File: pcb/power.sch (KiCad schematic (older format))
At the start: 25 parts, among them U16 AP22811AW5-7‎, U17 AP61302, U18 LP5907MFX-3.3, U4 AP61302

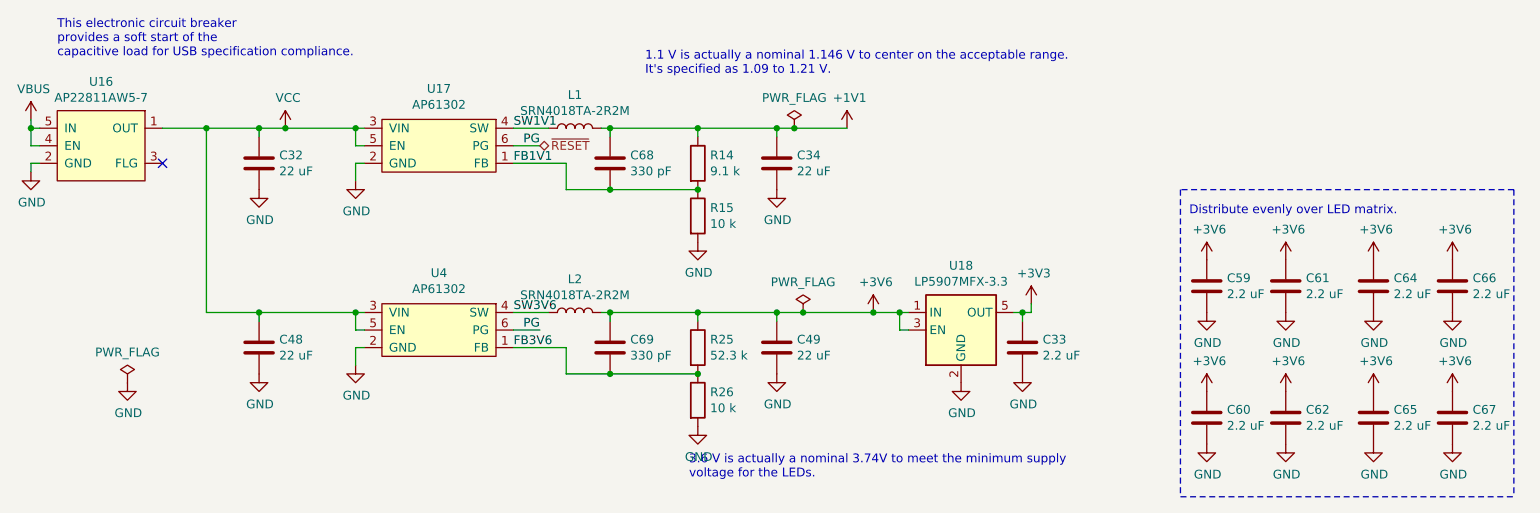
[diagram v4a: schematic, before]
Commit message: use AP3441LSHE-7B DC-DC switching to available part from long lead time part adds 2 22 uF 0805 capacitors as well
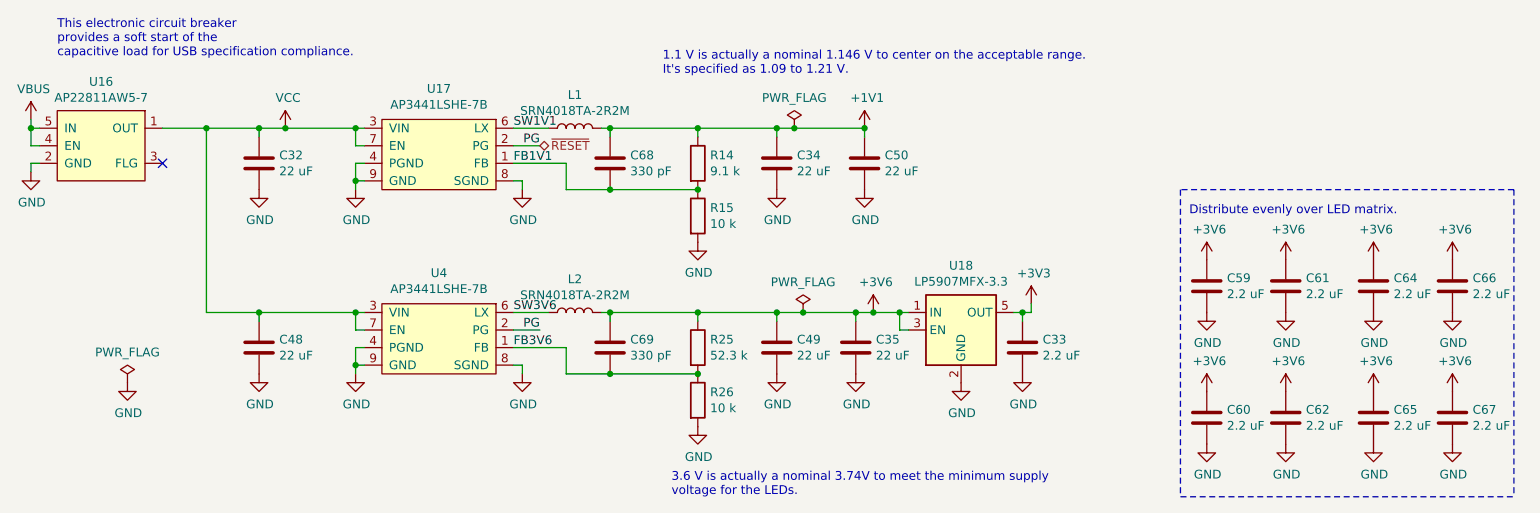
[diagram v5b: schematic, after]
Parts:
- removed U17, U4: AP61302, launch:SOT-563, symbol launch:AP61302
- added C35, C50: 22 uF, Capacitor_SMD:C_0805_2012Metric, symbol Device:C
- added U17, U4: AP3441LSHE-7B, launch:W-DFN2020-8_Type_C, symbol launch:AP3441LSHE-7B
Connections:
- net +1V1: now also C50.1
- net +3V6: now also C35.1
- net FB1V1: now also U17.1 (FB)
- net FB3V6: now also U4.1 (FB)
- net GND: now also C35.2, C50.2, U17.4 (PGND), U17.8 (SGND), U17.9 (GND), U4.4 (PGND), U4.8 (SGND), U4.9 (GND)
- net SW1V1: now also U17.6 (LX)
- net SW3V6: now also U4.6 (LX)
- net VCC: now also U17.3 (VIN), U17.7 (EN), U4.3 (VIN), U4.7 (EN)
- net ~RESET: now also U17.2 (PG), U4.2 (PG)
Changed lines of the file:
@@
 encoding utf-8
 Sheet 3 3
-Title ""
-Date "2021-05-27"
-Rev ""
-Comp ""
+Title "Launch"
+Date "2021-09-13"
+Rev "1.4"
+Comp "System76"
 Comment1 ""
 Comment2 ""
@@
 L power:GND #PWR0248
 U 1 1 5F8E3978
-P 4500 4600
-F 0 "#PWR0248" H 4500 4350 50  0001 C CNN
-F 1 "GND" H 4505 4427 50  0000 C CNN
-F 2 "" H 4500 4600 50  0001 C CNN
-F 3 "" H 4500 4600 50  0001 C CNN
-	1    4500 4600
+P 4500 4650
+F 0 "#PWR0248" H 4500 4400 50  0001 C CNN
+F 1 "GND" H 4505 4477 50  0000 C CNN
+F 2 "" H 4500 4650 50  0001 C CNN
+F 3 "" H 4500 4650 50  0001 C CNN
+	1    4500 4650
 	1    0    0    -1
 $EndComp
@@
 Text Label 5400 4500 0    50   ~ 0
 FB1V1
-Text Notes 6150 4000 0    50   ~ 0
+Text Notes 6250 4000 0    50   ~ 0
 1.1 V is actually a nominal 1.146 V to center on the acceptable range.\nIt's specified as 1.09 to 1.21 V.
 Connection ~ 3950 4300
@@
 $EndComp
 Connection ~ 4100 4300
-$Comp
-L power:GND #PWR0198
-U 1 1 604E7615
-P 4500 5650
-F 0 "#PWR0198" H 4500 5400 50  0001 C CNN
-F 1 "GND" H 4505 5477 50  0000 C CNN
-F 2 "" H 4500 5650 50  0001 C CNN
-F 3 "" H 4500 5650 50  0001 C CNN
-	1    4500 5650
-	1    0    0    -1
-$EndComp
-Wire Wire Line
-	4550 5550 4500 5550
 $Comp
 L Device:L L2
@@
 	1    0    0    -1
 $EndComp
-Text Notes 6400 6300 0    50   ~ 0
+Text Notes 6300 6400 0    50   ~ 0
 3.6 V is actually a nominal 3.74V to meet the minimum supply\nvoltage for the LEDs.
 $Comp
@@
 	4500 4500 4500 4600
 Wire Wire Line
-	4500 5550 4500 5650
-Wire Wire Line
 	5900 4300 5950 4300
 Wire Wire Line
@@
 	5700 5700 5950 5700
 $Comp
-L launch:AP61302 U17
-U 1 1 60AFBC5E
-P 4650 4250
-F 0 "U17" H 4975 4425 50  0000 C CNN
-F 1 "AP61302" H 4975 4334 50  0000 C CNN
-F 2 "launch:SOT-563" H 5000 4300 50  0001 L CNN
-F 3 "${KIPRJMOD}/docs/AP61302.pdf" V 4900 4250 50  0001 C CNN
-	1    4650 4250
-	1    0    0    -1
-$EndComp
-$Comp
 L power:+3V3 #PWR0257
 U 1 1 5F906CD9
@@
 	1    0    0    -1
 $EndComp
-Connection ~ 7000 4300
-Wire Wire Line
-	7000 4300 7300 4300
 $Comp
 L power:PWR_FLAG #FLG0101
@@
 L power:+1V1 #PWR0249
 U 1 1 5F8E3BF2
-P 7300 4300
-F 0 "#PWR0249" H 7300 4150 50  0001 C CNN
-F 1 "+1V1" H 7315 4473 50  0000 C CNN
-F 2 "" H 7300 4300 50  0001 C CNN
-F 3 "" H 7300 4300 50  0001 C CNN
-	1    7300 4300
-	1    0    0    -1
-$EndComp
-$Comp
-L launch:AP61302 U4
-U 1 1 60AFC5EA
-P 4650 5300
-F 0 "U4" H 4975 5475 50  0000 C CNN
-F 1 "AP61302" H 4975 5384 50  0000 C CNN
-F 2 "launch:SOT-563" H 5000 5350 50  0001 L CNN
-F 3 "${KIPRJMOD}/docs/AP61302.pdf" V 4900 5300 50  0001 C CNN
-	1    4650 5300
+P 7400 4300
+F 0 "#PWR0249" H 7400 4150 50  0001 C CNN
+F 1 "+1V1" H 7415 4473 50  0000 C CNN
+F 2 "" H 7400 4300 50  0001 C CNN
+F 3 "" H 7400 4300 50  0001 C CNN
+	1    7400 4300
 	1    0    0    -1
 $EndComp
@@
 $EndComp
 Wire Wire Line
-	7050 5350 7450 5350
+	7050 5350 7350 5350
 Wire Wire Line
 	5950 4300 6450 4300
@@
 Wire Wire Line
 	6450 4300 6900 4300
+$Comp
+L launch:AP3441LSHE-7B U17
+U 1 1 615E9120
+P 4650 4250
+F 0 "U17" H 4975 4425 50  0000 C CNN
+F 1 "AP3441LSHE-7B" H 4975 4334 50  0000 C CNN
+F 2 "launch:W-DFN2020-8_Type_C" H 4650 4300 50  0001 L CNN
+F 3 "${KIPRJMOD}/docs/AP3441-L.pdf" V 4900 4250 50  0001 C CNN
+	1    4650 4250
+	1    0    0    -1
+$EndComp
+Wire Wire Line
+	4550 4600 4500 4600
+Connection ~ 4500 4600
+Wire Wire Line
+	4500 4650 4500 4600
+$Comp
+L power:GND #PWR0198
+U 1 1 615F55C5
+P 5450 5700
+F 0 "#PWR0198" H 5450 5450 50  0001 C CNN
+F 1 "GND" H 5455 5527 50  0000 C CNN
+F 2 "" H 5450 5700 50  0001 C CNN
+F 3 "" H 5450 5700 50  0001 C CNN
+	1    5450 5700
+	1    0    0    -1
+$EndComp
+Wire Wire Line
+	5400 5650 5450 5650
+Wire Wire Line
+	5450 5650 5450 5700
+$Comp
+L power:GND #PWR0200
+U 1 1 615FFD5B
+P 4500 5700
+F 0 "#PWR0200" H 4500 5450 50  0001 C CNN
+F 1 "GND" H 4505 5527 50  0000 C CNN
+F 2 "" H 4500 5700 50  0001 C CNN
+F 3 "" H 4500 5700 50  0001 C CNN
+	1    4500 5700
+	1    0    0    -1
+$EndComp
+Wire Wire Line
+	4550 5550 4500 5550
+Wire Wire Line
+	4500 5550 4500 5650
+$Comp
+L launch:AP3441LSHE-7B U4
+U 1 1 615FFE7B
+P 4650 5300
+F 0 "U4" H 4975 5475 50  0000 C CNN
+F 1 "AP3441LSHE-7B" H 4975 5384 50  0000 C CNN
+F 2 "launch:W-DFN2020-8_Type_C" H 4650 5350 50  0001 L CNN
+F 3 "${KIPRJMOD}/docs/AP3441-L.pdf" V 4900 5300 50  0001 C CNN
+	1    4650 5300
+	1    0    0    -1
+$EndComp
+Wire Wire Line
+	4550 5650 4500 5650
+Connection ~ 4500 5650
+Wire Wire Line
+	4500 5700 4500 5650
+$Comp
+L power:GND #PWR0251
+U 1 1 616087A6
+P 5450 4650
+F 0 "#PWR0251" H 5450 4400 50  0001 C CNN
+F 1 "GND" H 5455 4477 50  0000 C CNN
+F 2 "" H 5450 4650 50  0001 C CNN
+F 3 "" H 5450 4650 50  0001 C CNN
+	1    5450 4650
+	1    0    0    -1
+$EndComp
+Wire Wire Line
+	5400 4600 5450 4600
+Wire Wire Line
+	5450 4600 5450 4650
+$Comp
+L Device:C C50
+U 1 1 6163DAB0
+P 7400 4500
+F 0 "C50" H 7515 4546 50  0000 L CNN
+F 1 "22 uF" H 7515 4455 50  0000 L CNN
+F 2 "Capacitor_SMD:C_0805_2012Metric" H 7438 4350 50  0001 C CNN
+F 3 "~" H 7400 4500 50  0001 C CNN
+F 4 "Generic X5R capacitor" H 7400 4500 50  0001 C CNN "Manufacturer"
+	1    7400 4500
+	1    0    0    -1
+$EndComp
+$Comp
+L power:GND #PWR0373
+U 1 1 6163DC80
+P 7400 4650
+F 0 "#PWR0373" H 7400 4400 50  0001 C CNN
+F 1 "GND" H 7405 4477 50  0000 C CNN
+F 2 "" H 7400 4650 50  0001 C CNN
+F 3 "" H 7400 4650 50  0001 C CNN
+	1    7400 4650
+	1    0    0    -1
+$EndComp
+$Comp
+L Device:C C35
+U 1 1 61641AF7
+P 7350 5550
+F 0 "C35" H 7465 5596 50  0000 L CNN
+F 1 "22 uF" H 7465 5505 50  0000 L CNN
+F 2 "Capacitor_SMD:C_0805_2012Metric" H 7388 5400 50  0001 C CNN
+F 3 "~" H 7350 5550 50  0001 C CNN
+F 4 "Generic X5R capacitor" H 7350 5550 50  0001 C CNN "Manufacturer"
+	1    7350 5550
+	1    0    0    -1
+$EndComp
+$Comp
+L power:GND #PWR0374
+U 1 1 61641CDD
+P 7350 5700
+F 0 "#PWR0374" H 7350 5450 50  0001 C CNN
+F 1 "GND" H 7355 5527 50  0000 C CNN
+F 2 "" H 7350 5700 50  0001 C CNN
+F 3 "" H 7350 5700 50  0001 C CNN
+	1    7350 5700
+	1    0    0    -1
+$EndComp
+Wire Wire Line
+	7400 4350 7400 4300
+Connection ~ 7400 4300
+Wire Wire Line
+	7000 4300 7400 4300
+Connection ~ 7000 4300
+Wire Wire Line
+	7350 5400 7350 5350
+Connection ~ 7350 5350
+Wire Wire Line
+	7350 5350 7450 5350
 $EndSCHEMATC
